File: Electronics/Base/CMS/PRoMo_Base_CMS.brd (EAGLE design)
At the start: 48 x 98 mm, 45 parts, among them IC1 DSPIC33FJ128MC804-PT, P1 Bornier, U1 CJ1117-3.3-1310190P1, U2 FT232R-SSOP28

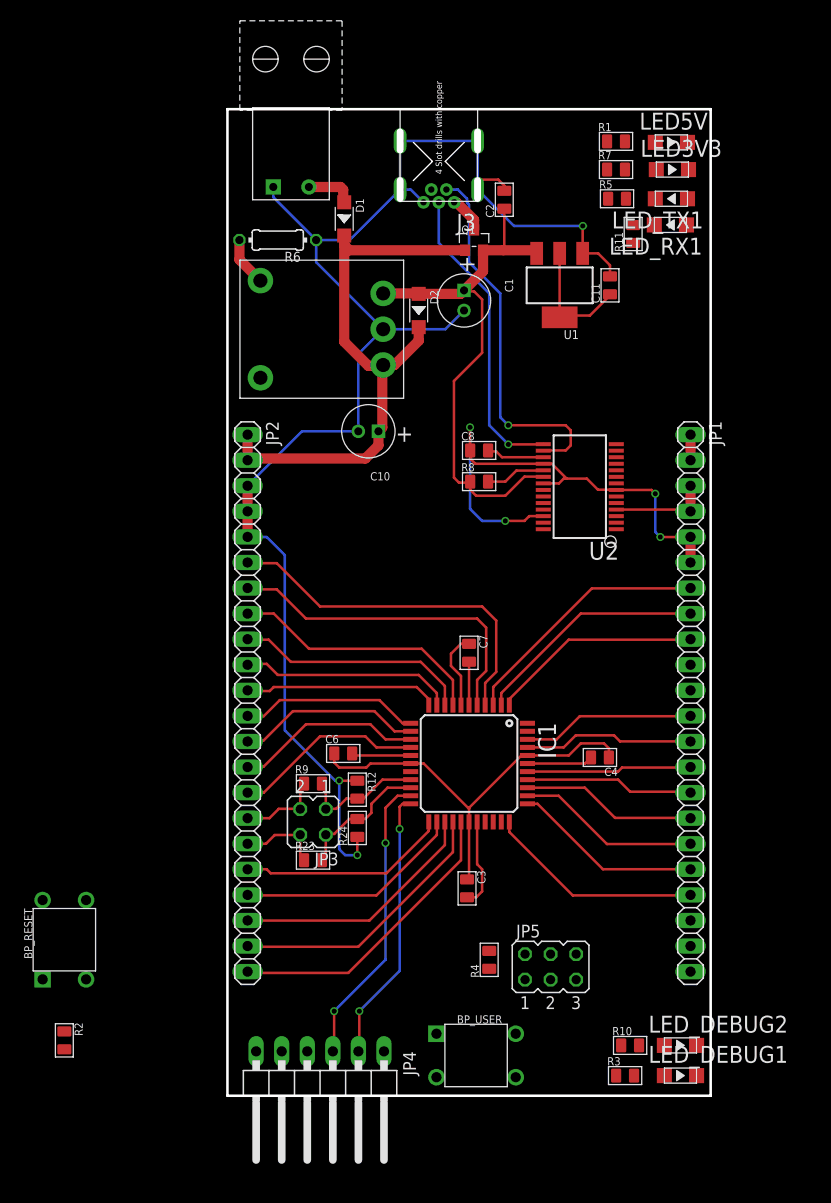
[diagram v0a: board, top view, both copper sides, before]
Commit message: Routage done, mais revoir schématique
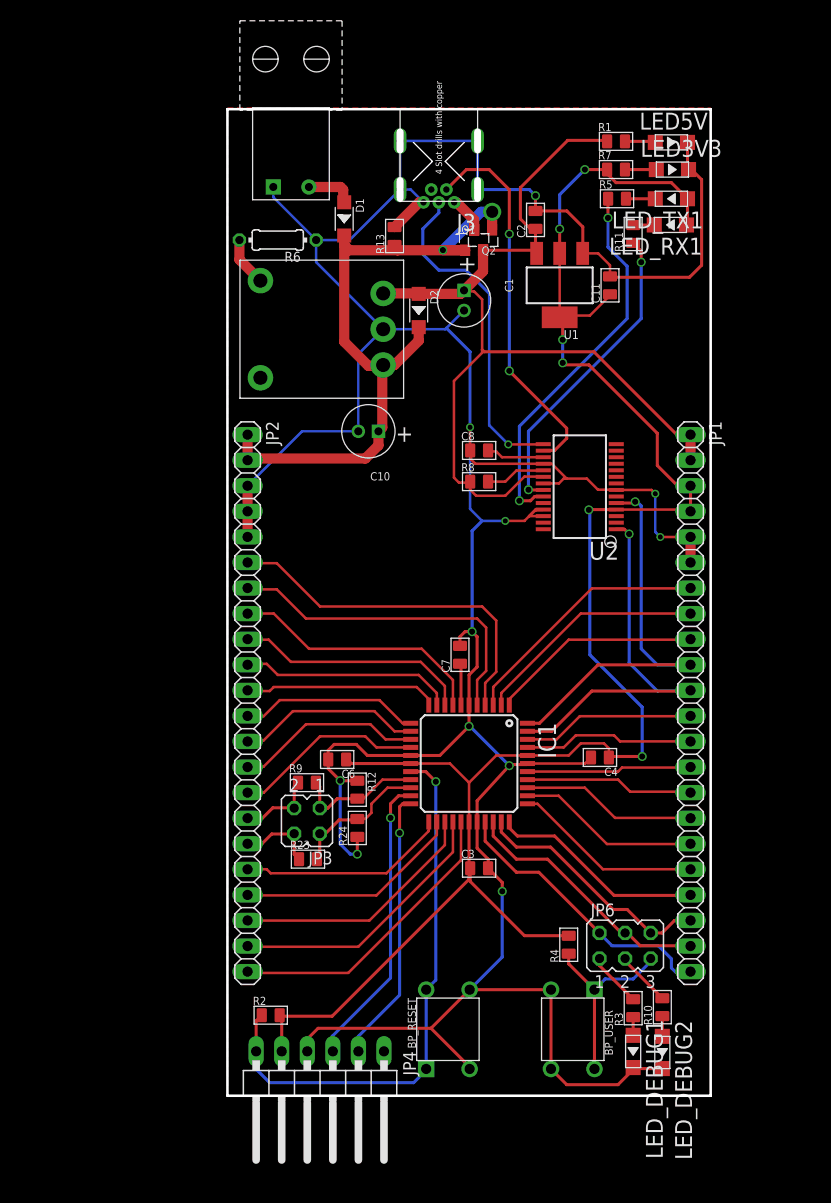
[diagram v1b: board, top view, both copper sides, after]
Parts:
- removed JP5: (no value), jumper:JP3Q
- added JP6: (no value), jumper:JP3Q
- added Q2: (no value), Discrete:SOT23
- added R13: 1M, Discrete:R0805
- moved BP_RESET 39.1 mm to (21.9, 6.60)
- moved R2 20.7 mm to (4.30, 8.00), turned to 0 degrees
- moved BP_USER 9.95 mm to (34.3, 6.60), turned to 270 degrees
- moved R4 8.04 mm to (33.9, 15.0)
- moved R3 6.75 mm to (40.3, 8.70), turned to 90 degrees
- moved LED_DEBUG1 5.28 mm to (40.3, 4.40), turned to 270 degrees
- moved R10 4.97 mm to (43.2, 8.80), turned to 90 degrees
- moved C2 3.69 mm to (30.6, 87.0)
- moved C3 2.33 mm to (25.0, 22.6), turned to 0 degrees
- moved LED_DEBUG2 1.93 mm to (43.2, 4.30), turned to 270 degrees
- moved C7 0.92 mm to (23.1, 43.8), turned to 90 degrees
- moved C6 0.85 mm to (10.9, 33.4), turned to 180 degrees
- moved JP3 0.61 mm to (7.90, 27.3)
- moved R9 0.61 mm to (7.90, 31.1)
- moved R23 0.51 mm to (8.00, 23.5)
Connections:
- net +5V: now also Q2.3
- net BP: now also JP6.3; no longer JP5.5
- net BP_USER/RA8: now also JP6.6; no longer JP5.6
- net LED_DEBUG1/RA2: now also JP6.4
- net LED_DEBUG2/RA3: now also JP6.5; no longer JP5.4
- net N$16: now also JP6.2; no longer JP5.3
- net N$6: now also JP6.1; no longer JP5.1
- net PE: now also R13.2
- net RX_FTDI: now also JP1.11; no longer JP1.10
- net TX_FTDI: now also JP1.10; no longer JP1.11
- net VIN: now also Q2.1, R13.1
- net VUSB: now also Q2.2
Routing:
- net +3V3: track 63.8 -> 184.1 mm, vias 0 -> 6
- net PE: track 230.0 -> 346.5 mm, vias 7 -> 11
- net !MCLR!: track 0.00 -> 55.6 mm, vias 0 -> 1
- net TX_FTDI: track 0.00 -> 41.1 mm, vias 0 -> 1
- net +5V: track 57.5 -> 98.1 mm
- net RX_FTDI: track 0.00 -> 39.4 mm, vias 0 -> 1
- net N$13: track 0.00 -> 37.8 mm, vias 0 -> 2
- net N$12: track 0.00 -> 31.0 mm, vias 0 -> 2
- net LED_DEBUG1/RA2: track 0.00 -> 28.2 mm
- net LED_DEBUG2/RA3: track 0.00 -> 25.5 mm
- net BP_USER/RA8: track 0.00 -> 24.5 mm
- net BP: track 0.00 -> 19.5 mm
- net VIN: track 57.8 -> 68.9 mm, vias 0 -> 2
- net N$16: track 0.00 -> 5.47 mm
- net N$6: track 0.00 -> 5.42 mm
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- added copper zone on layer 1, net PE
- added copper zone on layer 16, net PE
